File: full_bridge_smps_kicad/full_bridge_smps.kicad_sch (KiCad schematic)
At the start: 1 part, among them U1 UCC28950PW

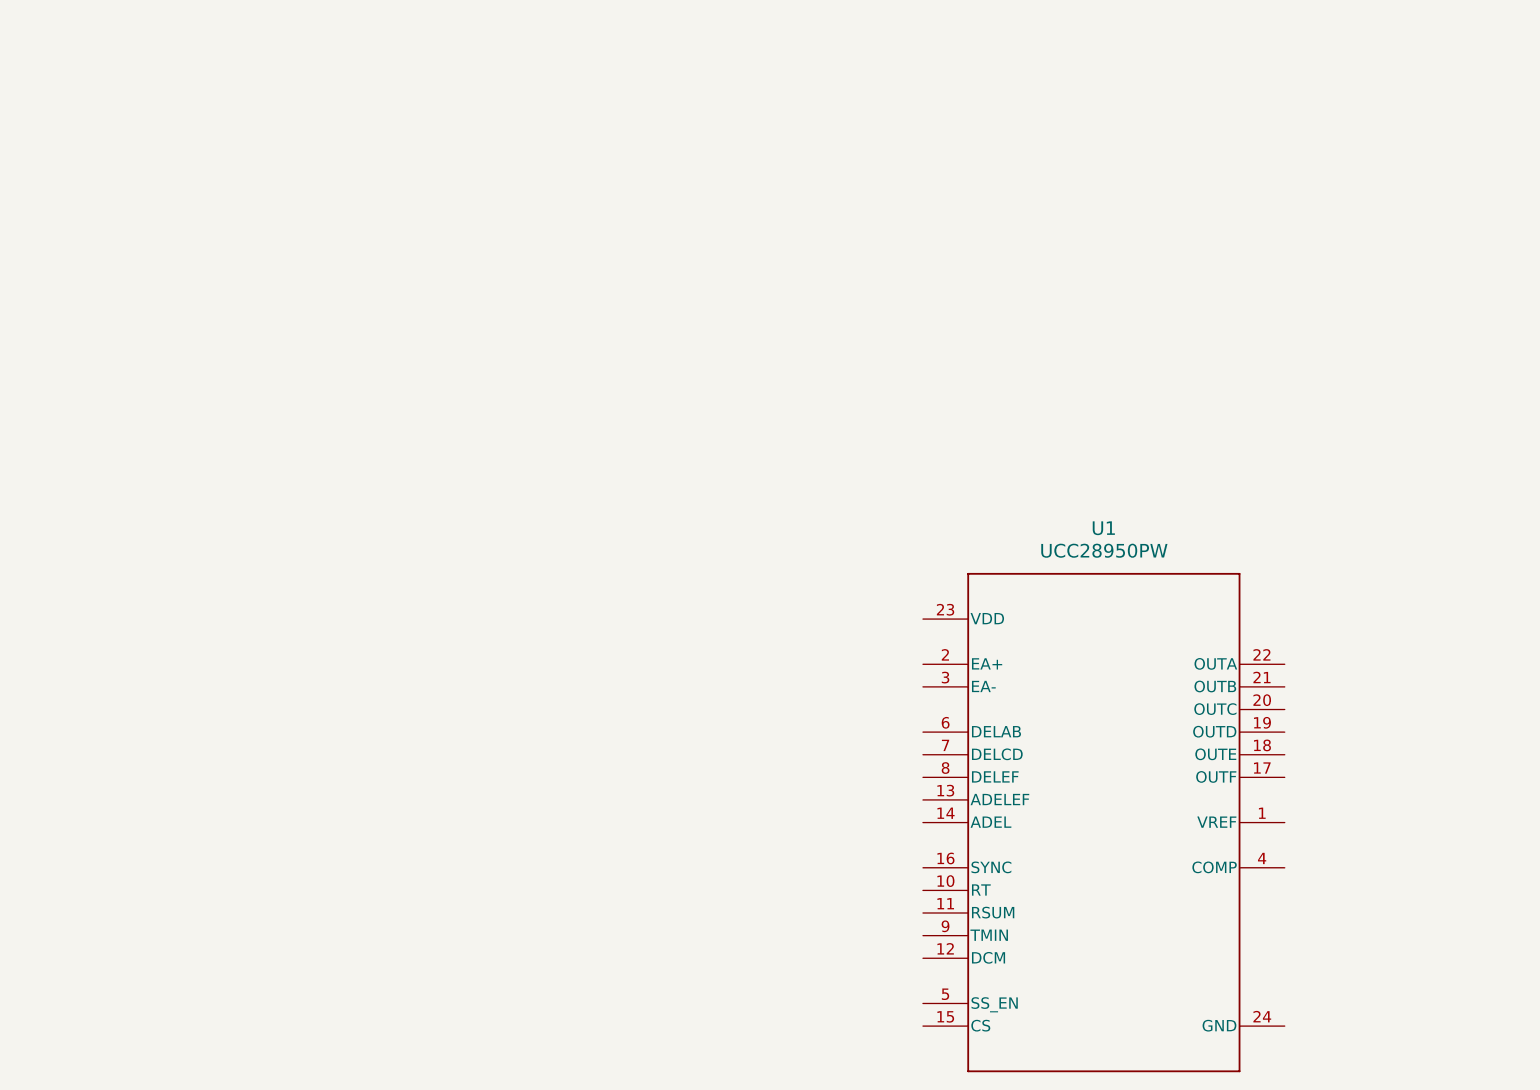
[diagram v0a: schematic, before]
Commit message: Saving work, getting the schematic clued up for the synchronous bridge converter
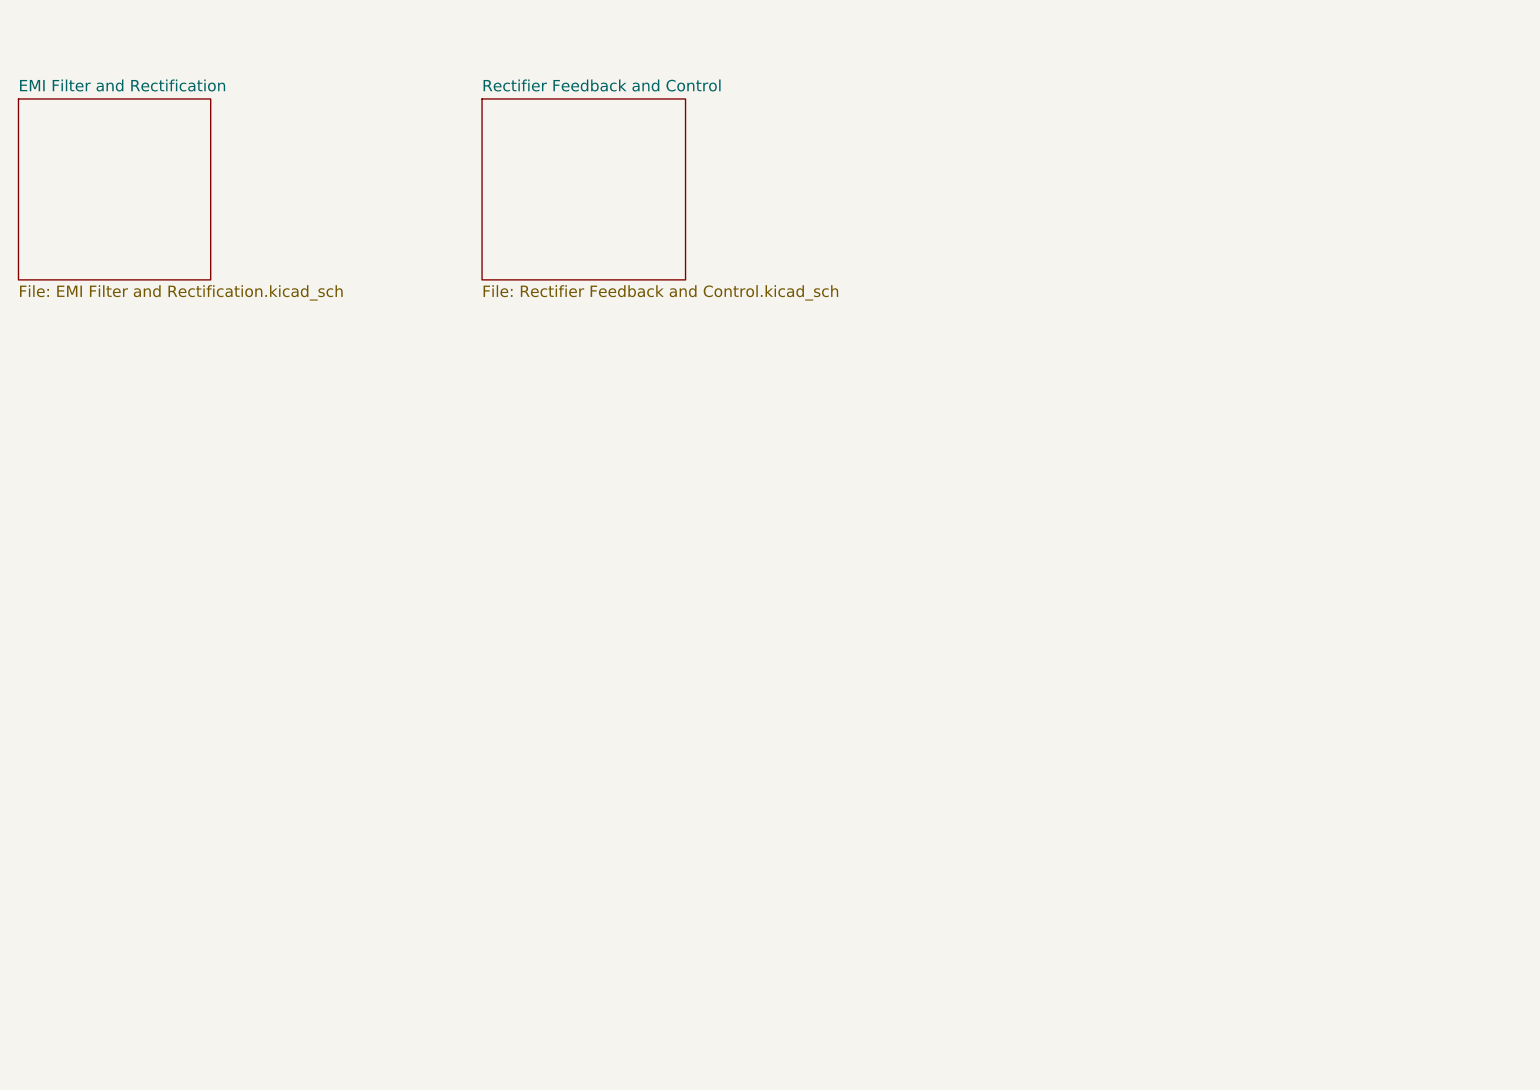
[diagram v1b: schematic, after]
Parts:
- removed U1: UCC28950PW, full bridge smps:UCC28950, symbol full bridge smps:UCC28950PW
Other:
- added sheet EMI Filter and Rectification (EMI Filter and Rectification.kicad_sch)
- added sheet Rectifier Feedback and Control (Rectifier Feedback and Control.kicad_sch)
- title: (none) -> Full Bridge SMPS
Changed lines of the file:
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@@
 (kicad_sch (version 20230121) (generator eeschema)
-  (paper "A4")
-  (symbol (lib_id "full bridge smps:UCC28950PW") (at 146.05 104.14 0) (unit 1)
-    (in_bom yes) (on_board yes) (dnp no) (fields_autoplaced)
-    (property "Reference" "U1" (at 146.05 71.12 0)
-      (effects (font (size 1.524 1.524)))
+  (paper "A5")
+  (title_block
+    (title "Full Bridge SMPS")
+    (rev "1.0.0")
+  )
+  (sheet (at 24.13 22.86) (size 21.59 20.32) (fields_autoplaced)
+    (stroke (width 0.1524) (type solid))
+    (fill (color 0 0 0 0.0000))
+    (property "Sheetname" "EMI Filter and Rectification" (at 24.13 22.1484 0)
+      (effects (font (size 1.27 1.27)) (justify left bottom))
     )
-    (property "Value" "UCC28950PW" (at 146.05 73.66 0)
-      (effects (font (size 1.524 1.524)))
+    (property "Sheetfile" "EMI Filter and Rectification.kicad_sch" (at 24.13 43.7646 0)
+      (effects (font (size 1.27 1.27)) (justify left top))
     )
-    (property "Footprint" "full bridge smps:UCC28950" (at 146.05 104.14 0)
-      (effects (font (size 1.27 1.27) italic) hide)
-    )
-    (property "Datasheet" "UCC28950PW" (at 146.05 104.14 0)
-      (effects (font (size 1.27 1.27) italic) hide)
-    )
-    (pin "7")
-    (pin "6")
-    (pin "4")
-    (pin "20")
-    (pin "5")
-    (pin "23")
-    (pin "8")
-    (pin "18")
-    (pin "2")
-    (pin "9")
-    (pin "17")
-    (pin "19")
-    (pin "3")
-    (pin "24")
-    (pin "10")
-    (pin "21")
-    (pin "11")
-    (pin "1")
-    (pin "16")
-    (pin "22")
-    (pin "15")
-    (pin "14")
-    (pin "12")
-    (pin "13")
     (instances
       (project "full_bridge_smps"
-        (path "/f89200e7-8fc9-4acb-bb2b-7da3a53d52f5"
-          (reference "U1") (unit 1)
-        )
+        (path "/f89200e7-8fc9-4acb-bb2b-7da3a53d52f5" (page "2"))
       )
     )
+  )
+  (sheet (at 76.2 22.86) (size 22.86 20.32) (fields_autoplaced)
+    (stroke (width 0.1524) (type solid))
+    (fill (color 0 0 0 0.0000))
+    (property "Sheetname" "Rectifier Feedback and Control" (at 76.2 22.1484 0)
+      (effects (font (size 1.27 1.27)) (justify left bottom))
+    )
+    (property "Sheetfile" "Rectifier Feedback and Control.kicad_sch" (at 76.2 43.7646 0)
+      (effects (font (size 1.27 1.27)) (justify left top))
+    )
+    (instances
+      (project "full_bridge_smps"
+        (path "/f89200e7-8fc9-4acb-bb2b-7da3a53d52f5" (page "3"))
+      )
+    )

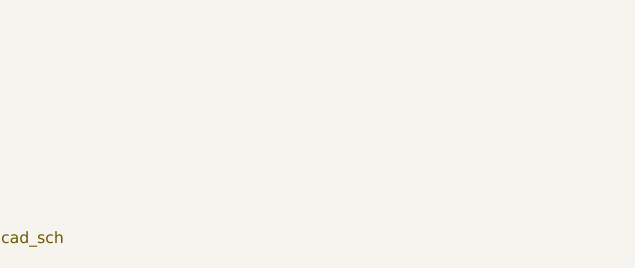
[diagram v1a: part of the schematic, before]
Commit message: Adding schematic page for interleaved CCM PFC
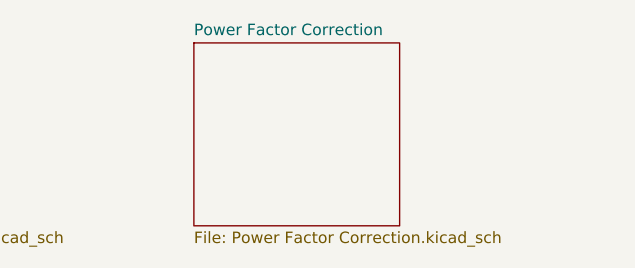
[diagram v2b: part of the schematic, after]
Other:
- added sheet Power Factor Correction (Power Factor Correction.kicad_sch)
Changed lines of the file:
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@@
+    )
+  )
+  (sheet (at 130.81 22.86) (size 22.86 20.32) (fields_autoplaced)
+    (stroke (width 0.1524) (type solid))
+    (fill (color 0 0 0 0.0000))
+    (property "Sheetname" "Power Factor Correction" (at 130.81 22.1484 0)
+      (effects (font (size 1.27 1.27)) (justify left bottom))
+    )
+    (property "Sheetfile" "Power Factor Correction.kicad_sch" (at 130.81 43.7646 0)
+      (effects (font (size 1.27 1.27)) (justify left top))
+    )
+    (instances
+      (project "full_bridge_smps"
+        (path "/f89200e7-8fc9-4acb-bb2b-7da3a53d52f5" (page "4"))
+      )
     )
   )

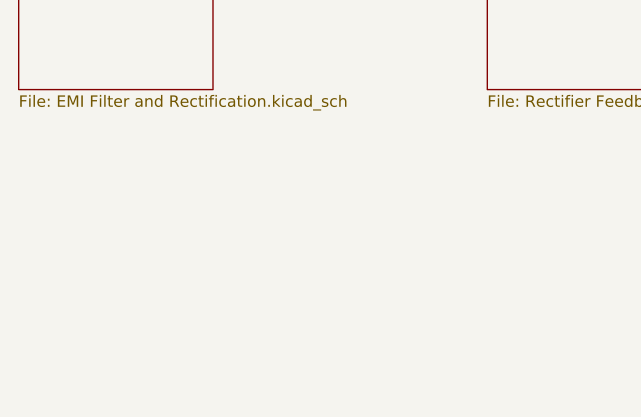
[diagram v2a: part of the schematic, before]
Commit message: Finishing power factor correction sheets, moving to power conversion
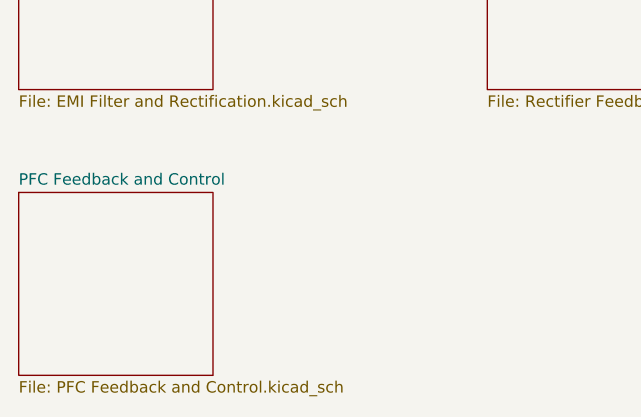
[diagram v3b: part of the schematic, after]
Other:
- added sheet PFC Feedback and Control (PFC Feedback and Control.kicad_sch)
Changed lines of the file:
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@@
+    )
+  )
+  (sheet (at 24.13 54.61) (size 21.59 20.32) (fields_autoplaced)
+    (stroke (width 0.1524) (type solid))
+    (fill (color 0 0 0 0.0000))
+    (property "Sheetname" "PFC Feedback and Control" (at 24.13 53.8984 0)
+      (effects (font (size 1.27 1.27)) (justify left bottom))
+    )
+    (property "Sheetfile" "PFC Feedback and Control.kicad_sch" (at 24.13 75.5146 0)
+      (effects (font (size 1.27 1.27)) (justify left top))
+    )
+    (instances
+      (project "full_bridge_smps"
+        (path "/f89200e7-8fc9-4acb-bb2b-7da3a53d52f5" (page "5"))
+      )
     )
   )

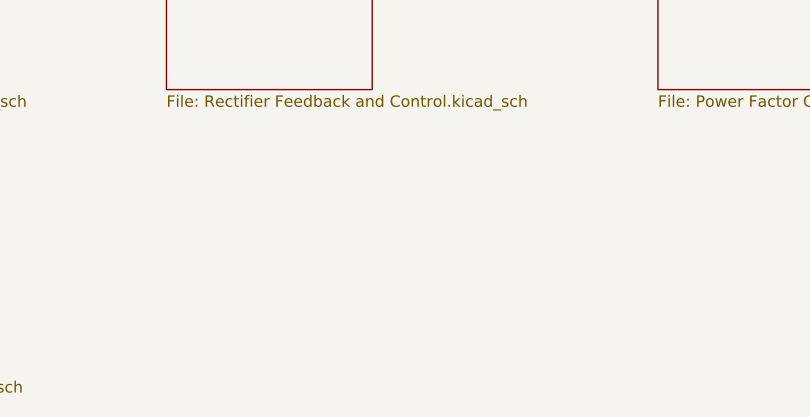
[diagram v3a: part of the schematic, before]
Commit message: Adding the full bridge power conversion
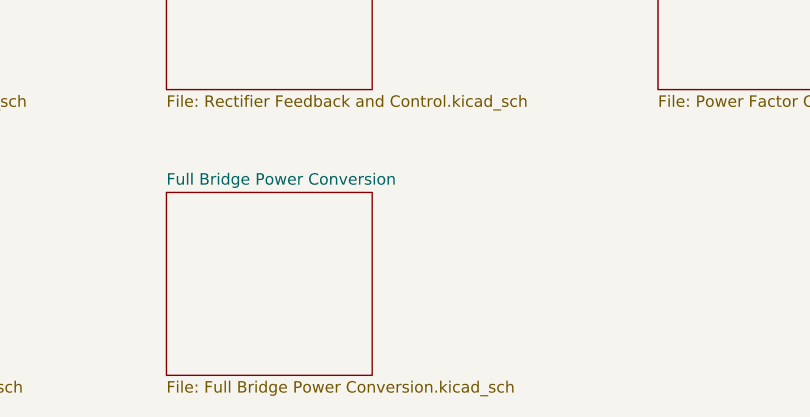
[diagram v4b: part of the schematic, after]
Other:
- added sheet Full Bridge Power Conversion (Full Bridge Power Conversion.kicad_sch)
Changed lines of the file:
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@@
+    )
+  )
+  (sheet (at 76.2 54.61) (size 22.86 20.32) (fields_autoplaced)
+    (stroke (width 0.1524) (type solid))
+    (fill (color 0 0 0 0.0000))
+    (property "Sheetname" "Full Bridge Power Conversion" (at 76.2 53.8984 0)
+      (effects (font (size 1.27 1.27)) (justify left bottom))
+    )
+    (property "Sheetfile" "Full Bridge Power Conversion.kicad_sch" (at 76.2 75.5146 0)
+      (effects (font (size 1.27 1.27)) (justify left top))
+    )
+    (instances
+      (project "full_bridge_smps"
+        (path "/f89200e7-8fc9-4acb-bb2b-7da3a53d52f5" (page "6"))
+      )
     )
   )
